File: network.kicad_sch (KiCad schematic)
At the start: 4 parts, among them J13 Conn_01x13, J14 Conn_01x12

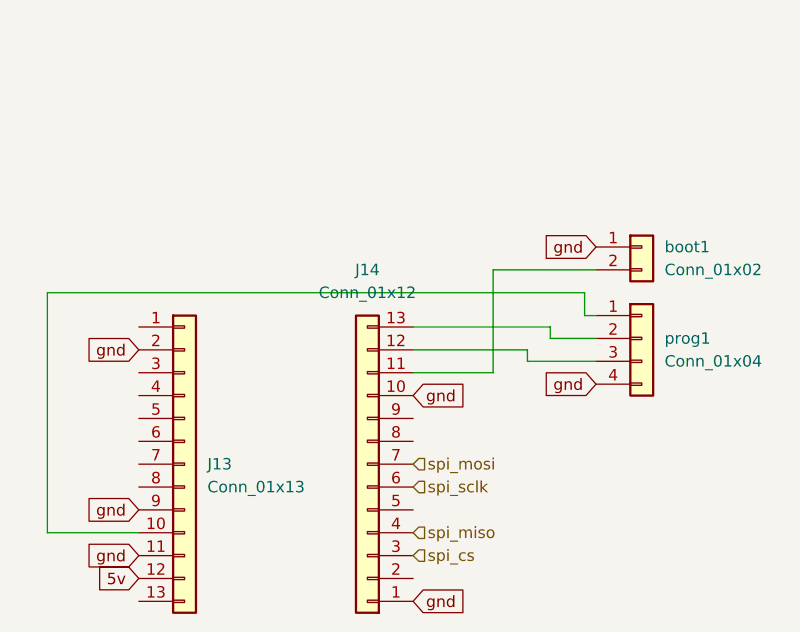
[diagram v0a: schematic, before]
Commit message: chaning network interface to W5500
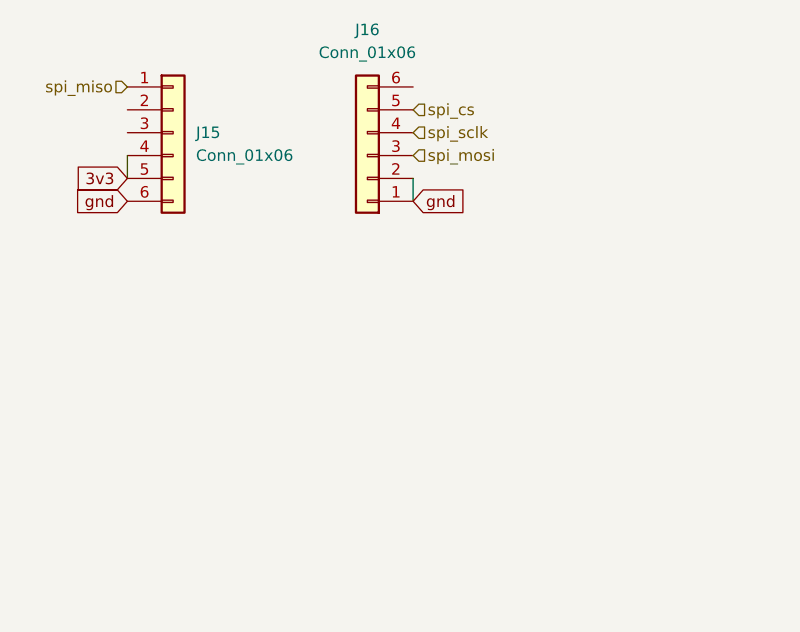
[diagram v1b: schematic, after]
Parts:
- removed J13: Conn_01x13, Connector_PinHeader_2.54mm:PinHeader_1x13_P2.54mm_Vertical, symbol Connector_Generic:Conn_01x13
- removed J14: Conn_01x12, Connector_PinHeader_2.54mm:PinHeader_1x13_P2.54mm_Vertical, symbol Connector_Generic:Conn_01x13
- removed boot1: Conn_01x02, Connector_PinHeader_2.54mm:PinHeader_1x02_P2.54mm_Vertical, symbol Connector_Generic:Conn_01x02
- removed prog1: Conn_01x04, Connector_PinHeader_2.54mm:PinHeader_1x04_P2.54mm_Vertical, symbol Connector_Generic:Conn_01x04
- added J15, J16: Conn_01x06, Connector_PinSocket_2.54mm:PinSocket_1x06_P2.54mm_Vertical, symbol Connector_Generic:Conn_01x06
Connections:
- net gnd: now also J15.6 (Pin_6), J16.1 (Pin_1), J16.2 (Pin_2)
- net spi_cs: now also J16.5 (Pin_5)
- net spi_miso: now also J15.1 (Pin_1)
- net spi_mosi: now also J16.3 (Pin_3)
- net spi_sclk: now also J16.4 (Pin_4)
- new net 3v3: J15.4 (Pin_4), J15.5 (Pin_5)
